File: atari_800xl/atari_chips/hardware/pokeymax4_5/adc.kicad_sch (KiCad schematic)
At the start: 8 parts

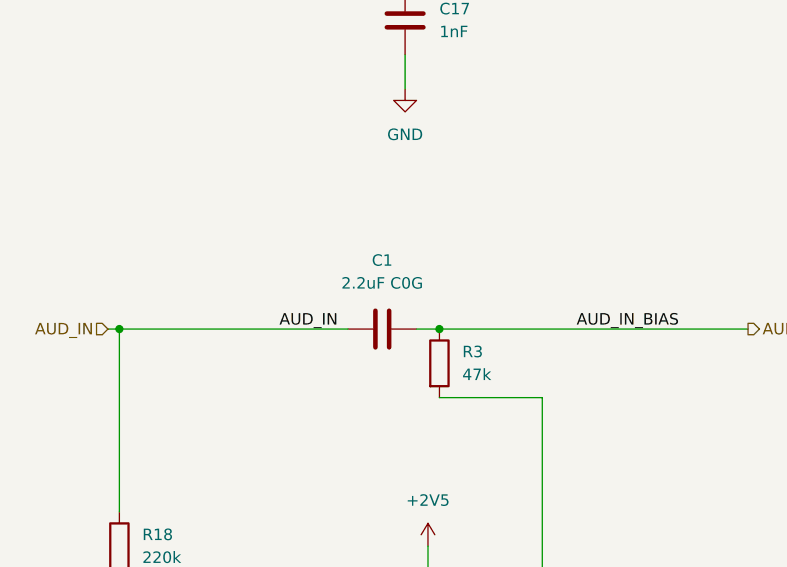
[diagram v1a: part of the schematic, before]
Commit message: 4.55. Got AI to help me improve a few minor things. Regulator mode, extra decoupling for DAC, distances from edge, gnd/power plane switched, track spacing for a few important lines, bigger cap on 2.5v reg, shorter critical traces on 3.3v reg. Also it double checked the sallen key filter. Switched to the JLCPCB plugin for simpler part management.
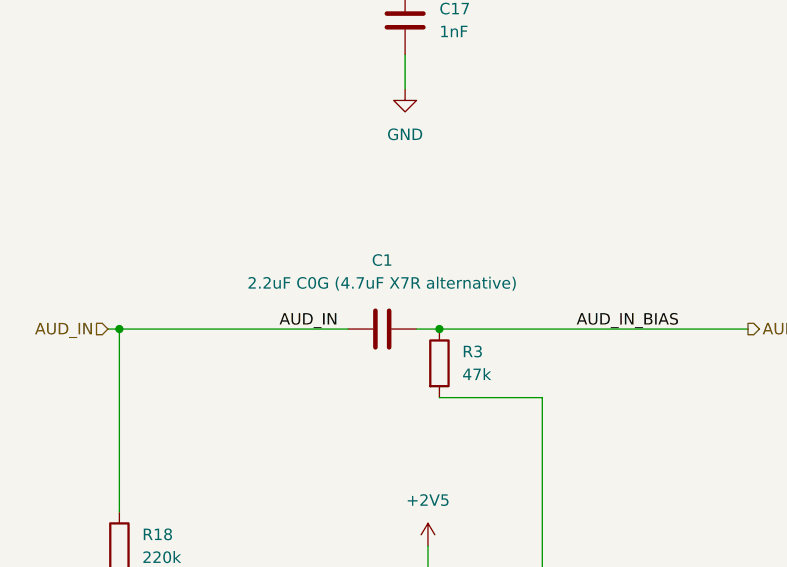
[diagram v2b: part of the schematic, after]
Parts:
- C1: value 2.2uF C0G -> 2.2uF C0G (4.7uF X7R alternative); LCSC (none) -> C5360844
- C17: LCSC (none) -> C126493
- C5: LCSC (none) -> C19702
- R18: LCSC (none) -> C22961
- R24: LCSC (none) -> C25860
- R3: LCSC (none) -> C25819
- R4: LCSC (none) -> C25804
- R5: LCSC (none) -> C137807
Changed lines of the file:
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@@
+			)
+		)
+		(property "LCSC" "C22961"
+			(at 33.02 116.84 0)
+			(hide yes)
+			(show_name no)
+			(do_not_autoplace no)
+			(effects
+				(font
+					(size 1.27 1.27)
+				)
 			)
 		)
@@
 			)
 		)
+		(property "LCSC" "C137807"
+			(at 67.31 123.19 0)
+			(hide yes)
+			(show_name no)
+			(do_not_autoplace no)
+			(effects
+				(font
+					(size 1.27 1.27)
+				)
+			)
+		)
 		(pin "1"
 		)
@@
 			)
 		)
+		(property "LCSC" "C25819"
+			(at 68.58 96.52 0)
+			(hide yes)
+			(show_name no)
+			(do_not_autoplace no)
+			(effects
+				(font
+					(size 1.27 1.27)
+				)
+			)
+		)
 		(pin "1"
 		)
@@
 			)
 		)
-		(property "Value" "2.2uF C0G"
+		(property "Value" "2.2uF C0G (4.7uF X7R alternative)"
 			(at 62.23 87.63 90)
 			(show_name no)
@@
 			)
 		)
+		(property "LCSC" "C5360844"
+			(at 62.23 92.71 0)
+			(hide yes)
+			(show_name no)
+			(do_not_autoplace no)
+			(effects
+				(font
+					(size 1.27 1.27)
+				)
+			)
+		)
 		(pin "1"
 		)
@@
 			)
 		)
+		(property "LCSC" "C25860"
+			(at 64.77 44.45 0)
+			(hide yes)
+			(show_name no)
+			(do_not_autoplace no)
+			(effects
+				(font
+					(size 1.27 1.27)
+				)
+			)
+		)
 		(pin "2"
 		)
@@
 			)
 		)
+		(property "LCSC" "C126493"
+			(at 64.77 58.42 0)
+			(hide yes)
+			(show_name no)
+			(do_not_autoplace no)
+			(effects
+				(font
+					(size 1.27 1.27)
+				)
+			)
+		)
 		(pin "1"
 		)
@@
 			)
 		)
+		(property "LCSC" "C19702"
+			(at 80.01 143.51 0)
+			(hide yes)
+			(show_name no)
+			(do_not_autoplace no)
+			(effects
+				(font
+					(size 1.27 1.27)
+				)
+			)
+		)
 		(pin "1"
 		)
@@
 			(at 67.31 143.51 0)
 			(hide yes)
+			(show_name no)
+			(do_not_autoplace no)
+			(effects
+				(font
+					(size 1.27 1.27)
+				)
+			)
+		)
+		(property "LCSC" "C25804"
+			(at 67.31 143.51 0)
+			(hide yes)
